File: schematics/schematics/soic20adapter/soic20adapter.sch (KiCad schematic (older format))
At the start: 3 parts, among them P1 DIL24, U1 SIL12, U2 SIL12

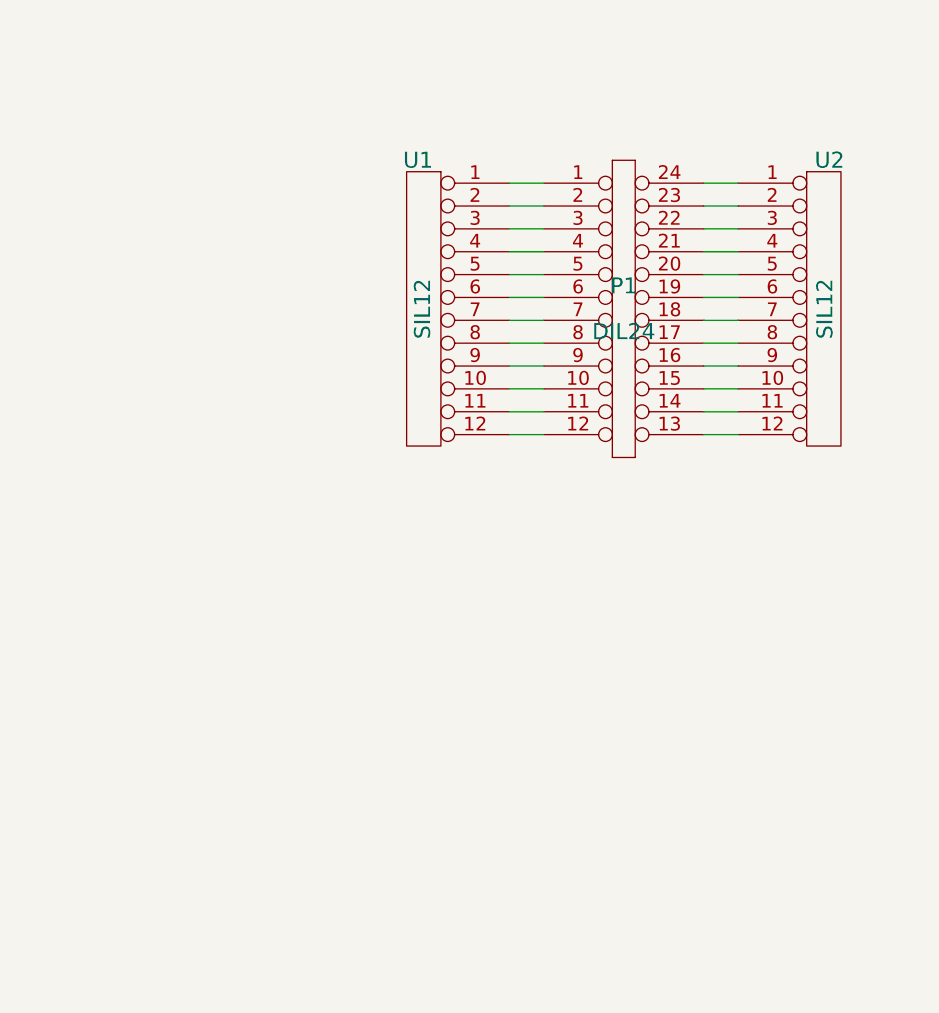
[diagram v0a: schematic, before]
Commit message: soic20 adapter board (4 pcs on a 5x5 cm)
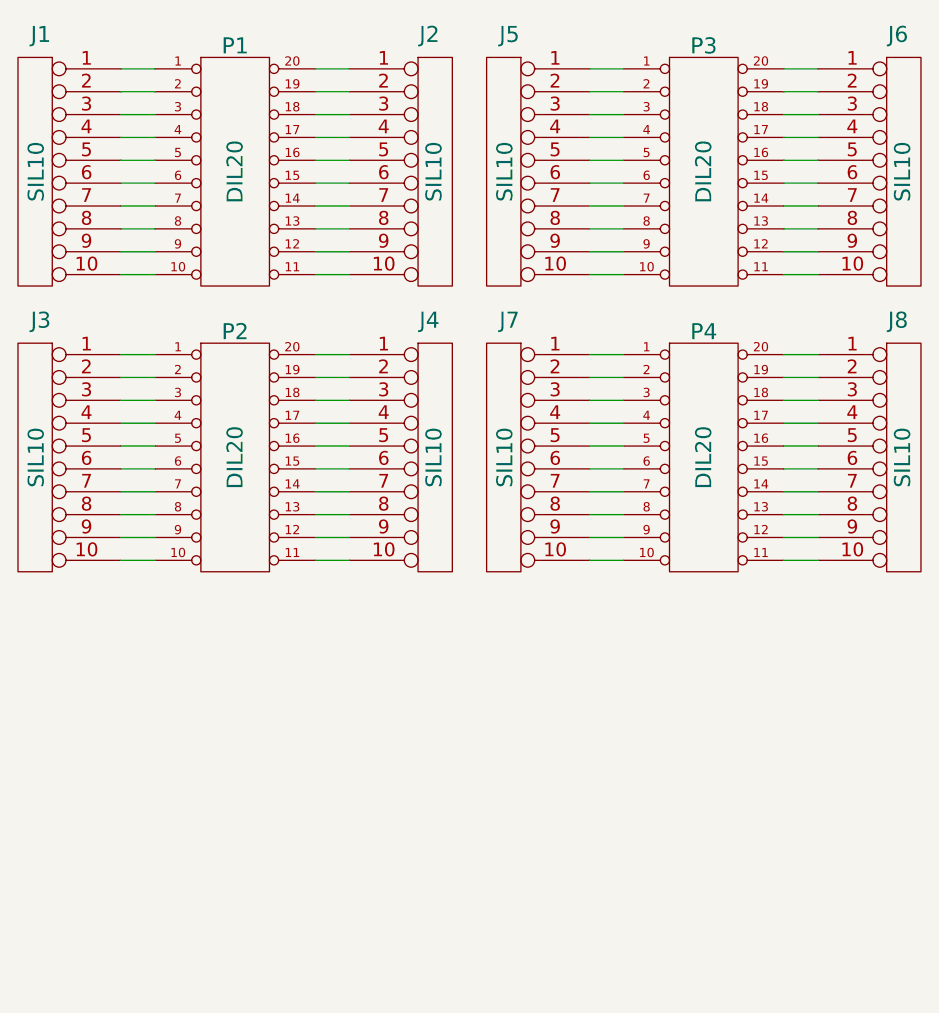
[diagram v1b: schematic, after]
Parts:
- removed P1: DIL24, symbol DIL24
- removed U1, U2: SIL12, symbol SIL12
- added J1, J2, J3, J4, J5, J6, J7, J8: SIL10, symbol SIL10
- added P1, P2, P3, P4: DIL20, symbol DIL20
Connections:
- new net: J1.1, P1.1 (P1)
- new net: J1.10, P1.10 (P10)
- new net: J2.10, P1.11 (P11)
- new net: J2.9, P1.12 (P12)
- new net: J2.8, P1.13 (P13)
- new net: J2.7, P1.14 (P14)
- new net: J2.6, P1.15 (P15)
- new net: J2.5, P1.16 (P16)
- new net: J2.4, P1.17 (P17)
- new net: J2.3, P1.18 (P18)
- new net: J2.2, P1.19 (P19)
- new net: J1.2, P1.2 (P2)
- new net: J2.1, P1.20 (P20)
- new net: J1.3, P1.3 (P3)
- new net: J1.4, P1.4 (P4)
- new net: J1.5, P1.5 (P5)
- new net: J1.6, P1.6 (P6)
- new net: J1.7, P1.7 (P7)
- new net: J1.8, P1.8 (P8)
- new net: J1.9, P1.9 (P9)
- new net: J4.1, P2.20 (P20)
- new net: J4.10, P2.11 (P11)
- new net: J4.2, P2.19 (P19)
- new net: J4.3, P2.18 (P18)
- new net: J4.4, P2.17 (P17)
- new net: J4.5, P2.16 (P16)
- new net: J4.6, P2.15 (P15)
- new net: J4.7, P2.14 (P14)
- new net: J4.8, P2.13 (P13)
- new net: J4.9, P2.12 (P12)
- new net: J3.1, P2.1 (P1)
- new net: J3.10, P2.10 (P10)
- new net: J3.2, P2.2 (P2)
- new net: J3.3, P2.3 (P3)
- new net: J3.4, P2.4 (P4)
- new net: J3.5, P2.5 (P5)
- new net: J3.6, P2.6 (P6)
- new net: J3.7, P2.7 (P7)
- new net: J3.8, P2.8 (P8)
- new net: J3.9, P2.9 (P9)
- new net: J7.1, P4.1 (P1)
- new net: J7.10, P4.10 (P10)
- new net: J8.10, P4.11 (P11)
- new net: J8.9, P4.12 (P12)
- new net: J8.8, P4.13 (P13)
- new net: J8.7, P4.14 (P14)
- new net: J8.6, P4.15 (P15)
- new net: J8.5, P4.16 (P16)
- new net: J8.4, P4.17 (P17)
- new net: J8.3, P4.18 (P18)
- new net: J8.2, P4.19 (P19)
- new net: J7.2, P4.2 (P2)
- new net: J8.1, P4.20 (P20)
- new net: J7.3, P4.3 (P3)
- new net: J7.4, P4.4 (P4)
- new net: J7.5, P4.5 (P5)
- new net: J7.6, P4.6 (P6)
- new net: J7.7, P4.7 (P7)
- new net: J7.8, P4.8 (P8)
- new net: J7.9, P4.9 (P9)
- new net: J6.1, P3.20 (P20)
- new net: J6.10, P3.11 (P11)
- new net: J6.2, P3.19 (P19)
- new net: J6.3, P3.18 (P18)
- new net: J6.4, P3.17 (P17)
- new net: J6.5, P3.16 (P16)
- new net: J6.6, P3.15 (P15)
- new net: J6.7, P3.14 (P14)
- new net: J6.8, P3.13 (P13)
- new net: J6.9, P3.12 (P12)
- new net: J5.1, P3.1 (P1)
- new net: J5.10, P3.10 (P10)
- new net: J5.2, P3.2 (P2)
- new net: J5.3, P3.3 (P3)
- new net: J5.4, P3.4 (P4)
- new net: J5.5, P3.5 (P5)
- new net: J5.6, P3.6 (P6)
- new net: J5.7, P3.7 (P7)
- new net: J5.8, P3.8 (P8)
- new net: J5.9, P3.9 (P9)

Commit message: soic adapter board
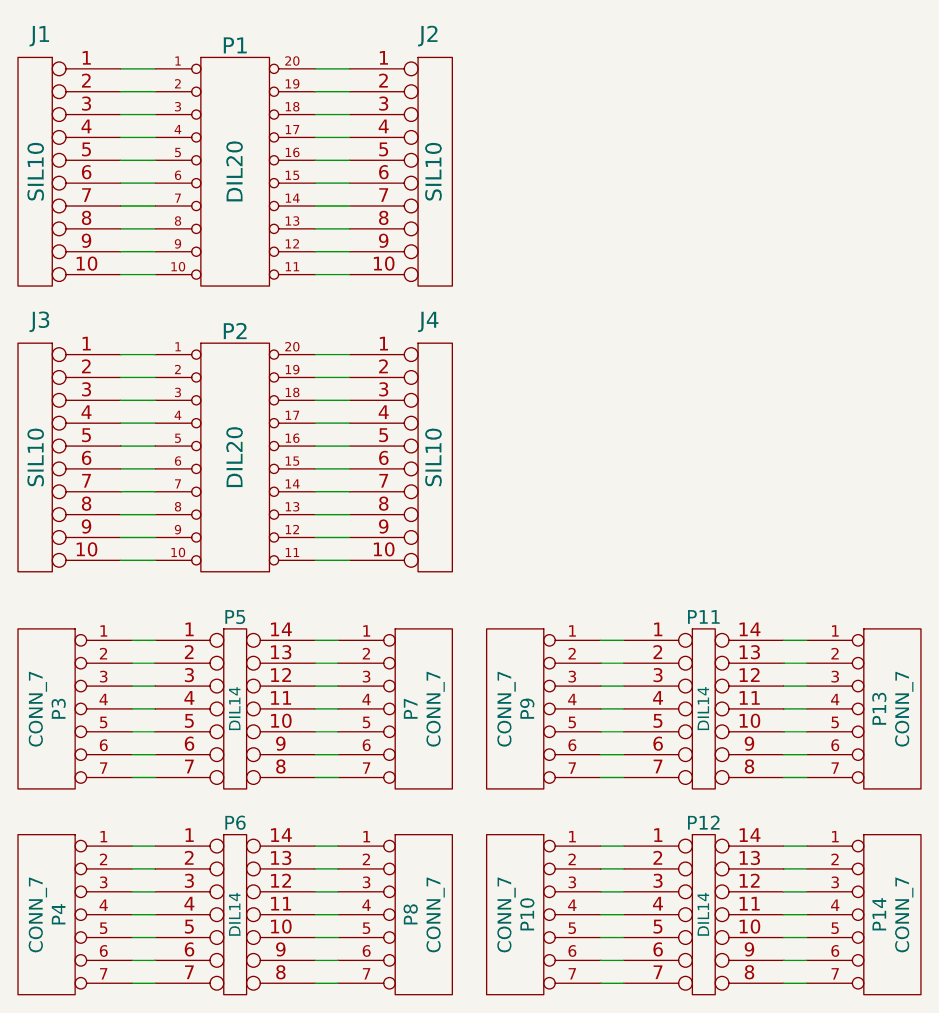
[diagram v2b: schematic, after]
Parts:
- removed J5, J6, J7, J8: SIL10, symbol SIL10
- removed P3, P4: DIL20, symbol DIL20
- added P10, P13, P14, P3, P4, P7, P8, P9: CONN_7, symbol CONN_7
- added P11, P12, P5, P6: DIL14, symbol DIL14
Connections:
- new net: P3.1 (P1), P5.1
- new net: P5.10, P7.5 (P5)
- new net: P5.11, P7.4 (P4)
- new net: P5.12, P7.3 (P3)
- new net: P5.13, P7.2 (P2)
- new net: P5.14, P7.1 (P1)
- new net: P3.2 (P2), P5.2
- new net: P3.3 (P3), P5.3
- new net: P3.4 (P4), P5.4
- new net: P3.5 (P5), P5.5
- new net: P3.6 (P6), P5.6
- new net: P3.7 (P7), P5.7
- new net: P5.8, P7.7 (P7)
- new net: P5.9, P7.6 (P6)
- new net: P11.14, P13.1 (P1)
- new net: P11.13, P13.2 (P2)
- new net: P11.12, P13.3 (P3)
- new net: P11.11, P13.4 (P4)
- new net: P11.10, P13.5 (P5)
- new net: P11.9, P13.6 (P6)
- new net: P11.8, P13.7 (P7)
- new net: P11.1, P9.1 (P1)
- new net: P11.2, P9.2 (P2)
- new net: P11.3, P9.3 (P3)
- new net: P11.4, P9.4 (P4)
- new net: P11.5, P9.5 (P5)
- new net: P11.6, P9.6 (P6)
- new net: P11.7, P9.7 (P7)
- new net: P4.1 (P1), P6.1
- new net: P6.10, P8.5 (P5)
- new net: P6.11, P8.4 (P4)
- new net: P6.12, P8.3 (P3)
- new net: P6.13, P8.2 (P2)
- new net: P6.14, P8.1 (P1)
- new net: P4.2 (P2), P6.2
- new net: P4.3 (P3), P6.3
- new net: P4.4 (P4), P6.4
- new net: P4.5 (P5), P6.5
- new net: P4.6 (P6), P6.6
- new net: P4.7 (P7), P6.7
- new net: P6.8, P8.7 (P7)
- new net: P6.9, P8.6 (P6)
- new net: P10.1 (P1), P12.1
- new net: P12.10, P14.5 (P5)
- new net: P12.11, P14.4 (P4)
- new net: P12.12, P14.3 (P3)
- new net: P12.13, P14.2 (P2)
- new net: P12.14, P14.1 (P1)
- new net: P10.2 (P2), P12.2
- new net: P10.3 (P3), P12.3
- new net: P10.4 (P4), P12.4
- new net: P10.5 (P5), P12.5
- new net: P10.6 (P6), P12.6
- new net: P10.7 (P7), P12.7
- new net: P12.8, P14.7 (P7)
- new net: P12.9, P14.6 (P6)
